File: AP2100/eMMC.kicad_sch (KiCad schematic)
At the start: 33 parts, among them U21 EMMC04G-M627-A01, U7 LS1043ASE7KQB-Layerscape

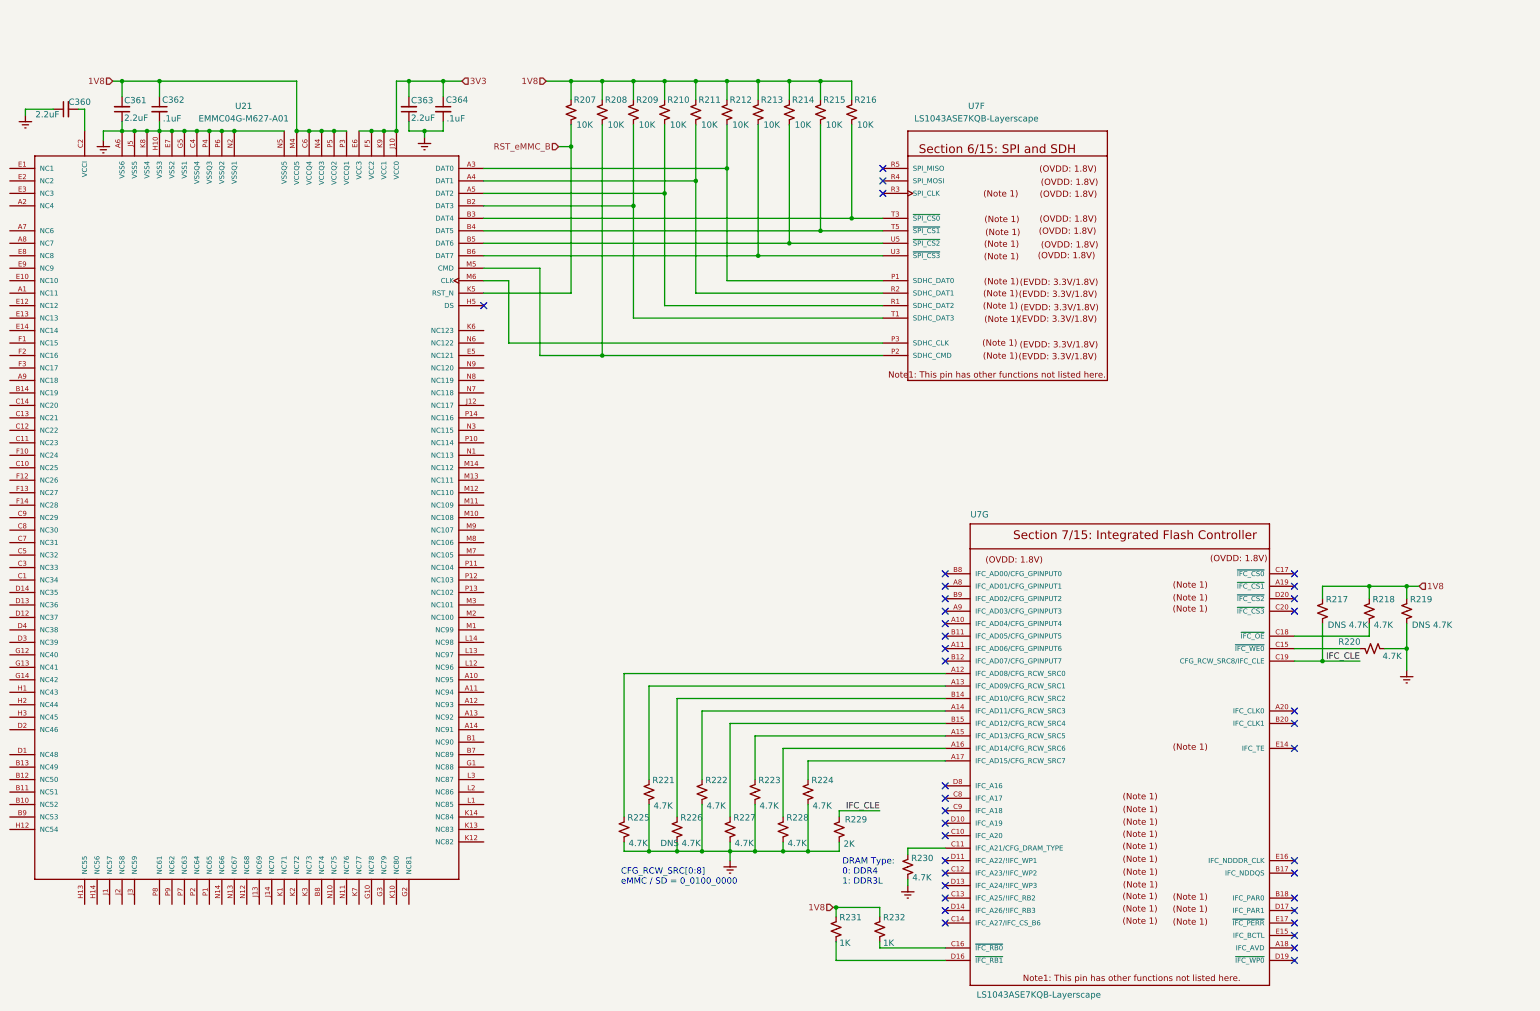
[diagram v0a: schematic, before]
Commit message: Added antenna mounting holes
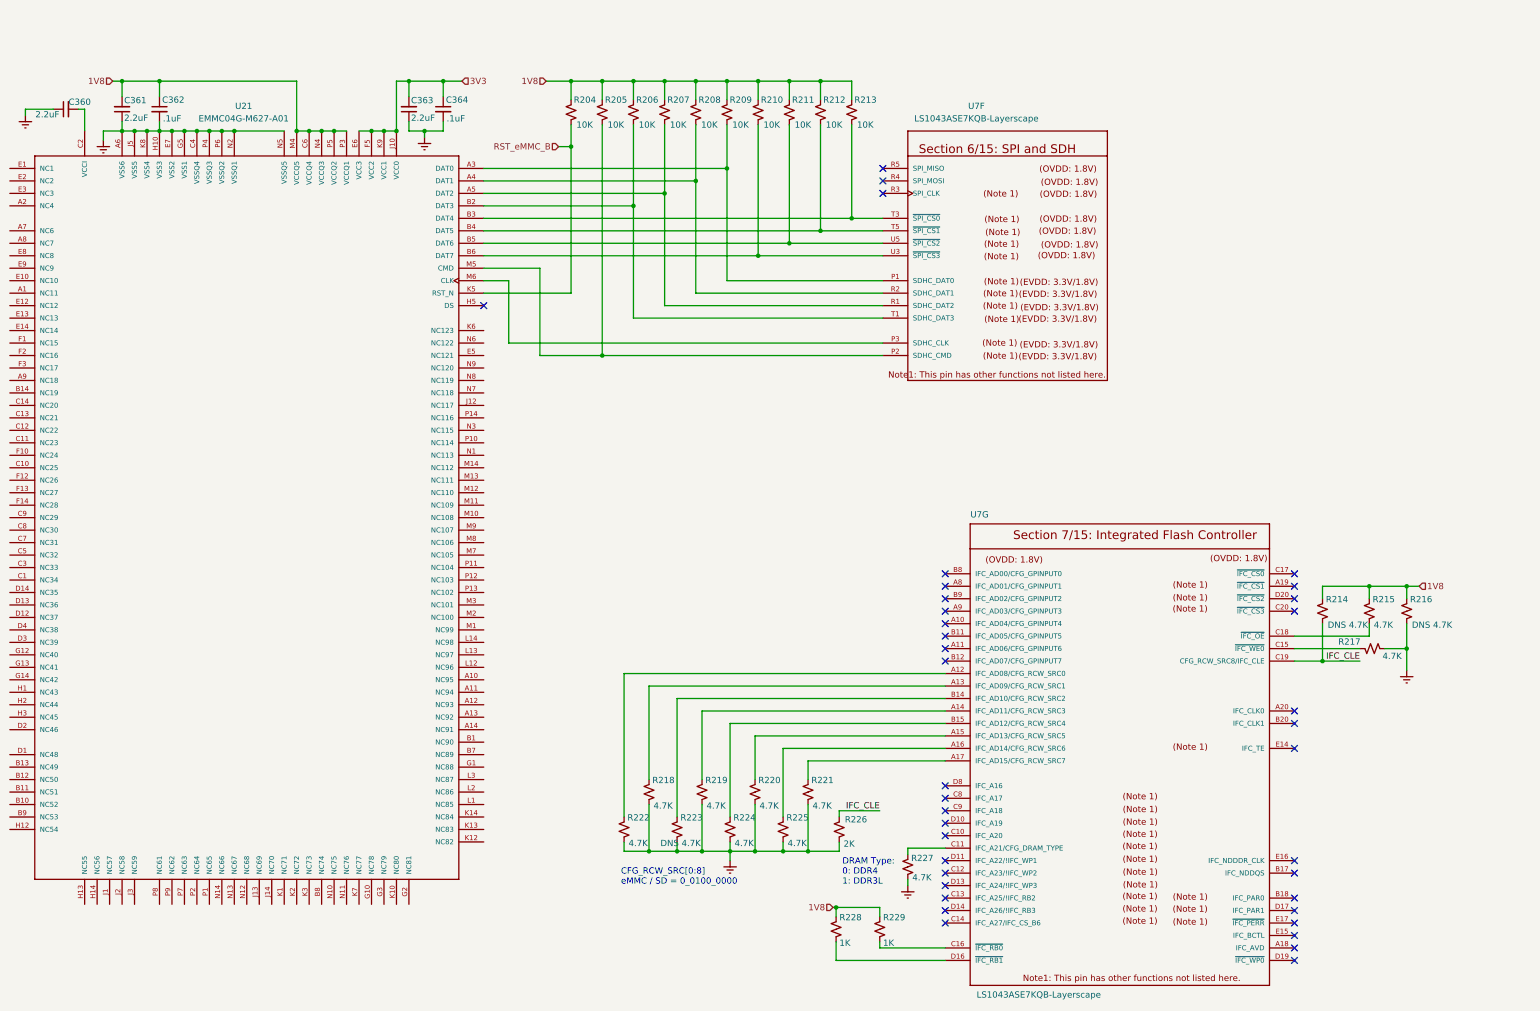
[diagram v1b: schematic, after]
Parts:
- renumbered R207 to R204, R208 to R205, R209 to R206, R210 to R207, R211 to R208, R212 to R209, R213 to R210, R214 to R211, R215 to R212, R216 to R213, R217 to R214, R218 to R215, R219 to R216, R220 to R217, R221 to R218, R222 to R219, R223 to R220, R224 to R221, R225 to R222, R226 to R223, R227 to R224, R228 to R225, R229 to R226, R230 to R227, R231 to R228, R232 to R229
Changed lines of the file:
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@@
   (symbol (lib_id "Device:R_Small_US") (at 167.64 46.99 0) (mirror y) (unit 1)
     (in_bom yes) (on_board yes)
-    (property "Reference" "R207" (id 0) (at 172.72 44.45 0)
+    (property "Reference" "R204" (id 0) (at 172.72 44.45 0)
       (effects (font (size 1.27 1.27)) (justify left))
     )
@@
   (symbol (lib_id "Device:R_Small_US") (at 173.99 46.99 0) (mirror y) (unit 1)
     (in_bom yes) (on_board yes)
-    (property "Reference" "R208" (id 0) (at 179.07 44.45 0)
+    (property "Reference" "R205" (id 0) (at 179.07 44.45 0)
       (effects (font (size 1.27 1.27)) (justify left))
     )
@@
   (symbol (lib_id "Device:R_Small_US") (at 178.435 193.04 0) (mirror y) (unit 1)
     (in_bom yes) (on_board yes)
-    (property "Reference" "R225" (id 0) (at 183.642 190.627 0)
+    (property "Reference" "R222" (id 0) (at 183.642 190.627 0)
       (effects (font (size 1.27 1.27)) (justify left))
     )
@@
   (symbol (lib_id "Device:R_Small_US") (at 180.34 46.99 0) (mirror y) (unit 1)
     (in_bom yes) (on_board yes)
-    (property "Reference" "R209" (id 0) (at 185.42 44.45 0)
+    (property "Reference" "R206" (id 0) (at 185.42 44.45 0)
       (effects (font (size 1.27 1.27)) (justify left))
     )
@@
   (symbol (lib_id "Device:R_Small_US") (at 183.515 185.42 0) (mirror y) (unit 1)
     (in_bom yes) (on_board yes)
-    (property "Reference" "R221" (id 0) (at 188.722 183.007 0)
+    (property "Reference" "R218" (id 0) (at 188.722 183.007 0)
       (effects (font (size 1.27 1.27)) (justify left))
     )
@@
   (symbol (lib_id "Device:R_Small_US") (at 186.69 46.99 0) (mirror y) (unit 1)
     (in_bom yes) (on_board yes)
-    (property "Reference" "R210" (id 0) (at 191.77 44.45 0)
+    (property "Reference" "R207" (id 0) (at 191.77 44.45 0)
       (effects (font (size 1.27 1.27)) (justify left))
     )
@@
   (symbol (lib_id "Device:R_Small_US") (at 189.23 193.04 0) (mirror y) (unit 1)
     (in_bom yes) (on_board yes)
-    (property "Reference" "R226" (id 0) (at 194.437 190.627 0)
+    (property "Reference" "R223" (id 0) (at 194.437 190.627 0)
       (effects (font (size 1.27 1.27)) (justify left))
     )
@@
   (symbol (lib_id "Device:R_Small_US") (at 193.04 46.99 0) (mirror y) (unit 1)
     (in_bom yes) (on_board yes)
-    (property "Reference" "R211" (id 0) (at 198.12 44.45 0)
+    (property "Reference" "R208" (id 0) (at 198.12 44.45 0)
       (effects (font (size 1.27 1.27)) (justify left))
     )
@@
   (symbol (lib_id "Device:R_Small_US") (at 194.31 185.42 0) (mirror y) (unit 1)
     (in_bom yes) (on_board yes)
-    (property "Reference" "R222" (id 0) (at 199.517 183.007 0)
+    (property "Reference" "R219" (id 0) (at 199.517 183.007 0)
       (effects (font (size 1.27 1.27)) (justify left))
     )
@@
   (symbol (lib_id "Device:R_Small_US") (at 199.39 46.99 0) (mirror y) (unit 1)
     (in_bom yes) (on_board yes)
-    (property "Reference" "R212" (id 0) (at 204.47 44.45 0)
+    (property "Reference" "R209" (id 0) (at 204.47 44.45 0)
       (effects (font (size 1.27 1.27)) (justify left))
     )
@@
   (symbol (lib_id "Device:R_Small_US") (at 200.025 193.04 0) (mirror y) (unit 1)
     (in_bom yes) (on_board yes)
-    (property "Reference" "R227" (id 0) (at 205.232 190.627 0)
+    (property "Reference" "R224" (id 0) (at 205.232 190.627 0)
       (effects (font (size 1.27 1.27)) (justify left))
     )
@@
   (symbol (lib_id "Device:R_Small_US") (at 205.105 185.42 0) (mirror y) (unit 1)
     (in_bom yes) (on_board yes)
-    (property "Reference" "R223" (id 0) (at 210.312 183.007 0)
+    (property "Reference" "R220" (id 0) (at 210.312 183.007 0)
       (effects (font (size 1.27 1.27)) (justify left))
     )
@@
   (symbol (lib_id "Device:R_Small_US") (at 205.74 46.99 0) (mirror y) (unit 1)
     (in_bom yes) (on_board yes)
-    (property "Reference" "R213" (id 0) (at 210.82 44.45 0)
+    (property "Reference" "R210" (id 0) (at 210.82 44.45 0)
       (effects (font (size 1.27 1.27)) (justify left))
     )
@@
   (symbol (lib_id "Device:R_Small_US") (at 210.82 193.04 0) (mirror y) (unit 1)
     (in_bom yes) (on_board yes)
-    (property "Reference" "R228" (id 0) (at 216.027 190.627 0)
+    (property "Reference" "R225" (id 0) (at 216.027 190.627 0)
       (effects (font (size 1.27 1.27)) (justify left))
     )
@@
   (symbol (lib_id "Device:R_Small_US") (at 212.09 46.99 0) (mirror y) (unit 1)
     (in_bom yes) (on_board yes)
-    (property "Reference" "R214" (id 0) (at 217.17 44.45 0)
+    (property "Reference" "R211" (id 0) (at 217.17 44.45 0)
       (effects (font (size 1.27 1.27)) (justify left))
     )
@@
   (symbol (lib_id "Device:R_Small_US") (at 215.9 185.42 0) (mirror y) (unit 1)
     (in_bom yes) (on_board yes)
-    (property "Reference" "R224" (id 0) (at 221.107 183.007 0)
+    (property "Reference" "R221" (id 0) (at 221.107 183.007 0)
       (effects (font (size 1.27 1.27)) (justify left))
     )
@@
   (symbol (lib_id "Device:R_Small_US") (at 218.44 46.99 0) (mirror y) (unit 1)
     (in_bom yes) (on_board yes)
-    (property "Reference" "R215" (id 0) (at 223.52 44.45 0)
+    (property "Reference" "R212" (id 0) (at 223.52 44.45 0)
       (effects (font (size 1.27 1.27)) (justify left))
     )
@@
   (symbol (lib_id "Device:R_Small_US") (at 221.615 213.36 0) (mirror y) (unit 1)
     (in_bom yes) (on_board yes)
-    (property "Reference" "R231" (id 0) (at 226.822 210.947 0)
+    (property "Reference" "R228" (id 0) (at 226.822 210.947 0)
       (effects (font (size 1.27 1.27)) (justify left))
     )
@@
   (symbol (lib_id "Device:R_Small_US") (at 222.25 193.04 0) (mirror x) (unit 1)
     (in_bom yes) (on_board yes)
-    (property "Reference" "R229" (id 0) (at 223.393 191.008 0)
+    (property "Reference" "R226" (id 0) (at 223.393 191.008 0)
       (effects (font (size 1.27 1.27)) (justify left))
     )
@@
   (symbol (lib_id "Device:R_Small_US") (at 224.79 46.99 0) (mirror y) (unit 1)
     (in_bom yes) (on_board yes)
-    (property "Reference" "R216" (id 0) (at 229.87 44.45 0)
+    (property "Reference" "R213" (id 0) (at 229.87 44.45 0)
       (effects (font (size 1.27 1.27)) (justify left))
     )
@@
   (symbol (lib_id "Device:R_Small_US") (at 230.505 213.36 0) (mirror y) (unit 1)
     (in_bom yes) (on_board yes)
-    (property "Reference" "R232" (id 0) (at 235.712 210.947 0)
+    (property "Reference" "R229" (id 0) (at 235.712 210.947 0)
       (effects (font (size 1.27 1.27)) (justify left))
     )
@@
   (symbol (lib_id "Device:R_Small_US") (at 236.22 200.66 0) (mirror y) (unit 1)
     (in_bom yes) (on_board yes)
-    (property "Reference" "R230" (id 0) (at 241.427 198.882 0)
+    (property "Reference" "R227" (id 0) (at 241.427 198.882 0)
       (effects (font (size 1.27 1.27)) (justify left))
     )
@@
   (symbol (lib_id "Device:R_Small_US") (at 320.675 148.59 0) (mirror y) (unit 1)
     (in_bom yes) (on_board yes)
-    (property "Reference" "R217" (id 0) (at 325.882 146.177 0)
+    (property "Reference" "R214" (id 0) (at 325.882 146.177 0)
       (effects (font (size 1.27 1.27)) (justify left))
     )
@@
   (symbol (lib_id "Device:R_Small_US") (at 330.2 148.59 0) (mirror y) (unit 1)
     (in_bom yes) (on_board yes)
-    (property "Reference" "R218" (id 0) (at 335.407 146.177 0)
+    (property "Reference" "R215" (id 0) (at 335.407 146.177 0)
       (effects (font (size 1.27 1.27)) (justify left))
     )
@@
   (symbol (lib_id "Device:R_Small_US") (at 330.835 156.21 90) (mirror x) (unit 1)
     (in_bom yes) (on_board yes)
-    (property "Reference" "R220" (id 0) (at 328.422 154.813 90)
+    (property "Reference" "R217" (id 0) (at 328.422 154.813 90)
       (effects (font (size 1.27 1.27)) (justify left))
     )
@@
   (symbol (lib_id "Device:R_Small_US") (at 337.82 148.59 0) (mirror y) (unit 1)
     (in_bom yes) (on_board yes)
-    (property "Reference" "R219" (id 0) (at 343.027 146.177 0)
-      (effects (font (size 1.27 1.27)) (justify left))
-    )
+    (property "Reference" "R216" (id 0) (at 343.027 146.177 0)
+      (effects (font (size 1.27 1.27)) (justify left))
+    )

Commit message: More cleanups
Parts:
- renumbered C360 to C378, C361 to C379, C362 to C380, C363 to C381, C364 to C382, R204 to R205, R205 to R206, R206 to R207, R207 to R208, R208 to R209, R209 to R210, R210 to R211, R211 to R212, R212 to R213, R213 to R214, R214 to R215, R215 to R216, R216 to R217, R217 to R218, R218 to R219, R219 to R220, R220 to R221, R221 to R222, R222 to R223, R223 to R224, R224 to R225, R225 to R226, R226 to R227, R227 to R228, R228 to R229, R229 to R230

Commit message: Not sure
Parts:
- U21: PartsBoxID (none) -> EMMC04G-M627-A01
- U7: value LS1043ASE7KQB-Layerscape -> LS1043ASE7xxx; PartsBoxID (none) -> LS1043ASE7
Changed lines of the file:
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@@
   (junction (at 337.82 143.51) (diameter 0.9144) (color 0 0 0 0))
   (junction (at 337.82 156.21) (diameter 0.9144) (color 0 0 0 0))
+  (no_connect (at 243.84 194.31))
+  (no_connect (at 314.96 143.51))
+  (no_connect (at 243.84 140.97))
+  (no_connect (at 243.84 143.51))
+  (no_connect (at 314.96 212.09))
+  (no_connect (at 231.14 58.42))
+  (no_connect (at 314.96 168.91))
+  (no_connect (at 243.84 156.21))
+  (no_connect (at 243.84 201.93))
+  (no_connect (at 314.96 219.71))
+  (no_connect (at 243.84 146.05))
+  (no_connect (at 243.84 191.77))
+  (no_connect (at 314.96 217.17))
+  (no_connect (at 231.14 63.5))
+  (no_connect (at 243.84 186.69))
+  (no_connect (at 243.84 158.75))
+  (no_connect (at 243.84 204.47))
+  (no_connect (at 243.84 184.15))
+  (no_connect (at 243.84 209.55))
+  (no_connect (at 314.96 199.39))
+  (no_connect (at 314.96 176.53))
+  (no_connect (at 231.14 60.96))
+  (no_connect (at 243.84 148.59))
+  (no_connect (at 314.96 148.59))
+  (no_connect (at 149.86 86.36))
+  (no_connect (at 243.84 189.23))
+  (no_connect (at 314.96 209.55))
+  (no_connect (at 243.84 212.09))
+  (no_connect (at 314.96 207.01))
+  (no_connect (at 243.84 207.01))
+  (no_connect (at 243.84 153.67))
+  (no_connect (at 243.84 151.13))
+  (no_connect (at 314.96 201.93))
+  (no_connect (at 314.96 146.05))
+  (no_connect (at 243.84 199.39))
+  (no_connect (at 314.96 214.63))
+  (no_connect (at 314.96 140.97))
   (no_connect (at 314.96 171.45))
-  (no_connect (at 314.96 146.05))
-  (no_connect (at 243.84 194.31))
-  (no_connect (at 314.96 199.39))
-  (no_connect (at 314.96 209.55))
-  (no_connect (at 243.84 158.75))
-  (no_connect (at 314.96 148.59))
-  (no_connect (at 314.96 217.17))
-  (no_connect (at 243.84 189.23))
-  (no_connect (at 314.96 212.09))
-  (no_connect (at 243.84 209.55))
-  (no_connect (at 314.96 207.01))
-  (no_connect (at 243.84 143.51))
-  (no_connect (at 243.84 201.93))
-  (no_connect (at 243.84 186.69))
-  (no_connect (at 243.84 153.67))
-  (no_connect (at 243.84 207.01))
-  (no_connect (at 243.84 191.77))
-  (no_connect (at 314.96 168.91))
-  (no_connect (at 243.84 151.13))
-  (no_connect (at 314.96 140.97))
-  (no_connect (at 314.96 143.51))
-  (no_connect (at 243.84 204.47))
-  (no_connect (at 314.96 176.53))
-  (no_connect (at 314.96 214.63))
-  (no_connect (at 243.84 184.15))
-  (no_connect (at 243.84 148.59))
-  (no_connect (at 231.14 63.5))
-  (no_connect (at 243.84 199.39))
-  (no_connect (at 314.96 219.71))
-  (no_connect (at 243.84 140.97))
-  (no_connect (at 314.96 201.93))
-  (no_connect (at 149.86 86.36))
-  (no_connect (at 243.84 212.09))
-  (no_connect (at 243.84 156.21))
-  (no_connect (at 243.84 146.05))
-  (no_connect (at 231.14 58.42))
-  (no_connect (at 231.14 60.96))
   (wire (pts (xy 56.515 46.355) (xy 56.515 47.625))
     (stroke (width 0) (type solid) (color 0 0 0 0))
@@
     (in_bom yes) (on_board yes)
     (property "Reference" "U7" (id 0) (at 250.19 45.72 0))
-    (property "Value" "LS1043ASE7KQB-Layerscape" (id 1) (at 250.19 48.26 0))
+    (property "Value" "LS1043ASE7xxx" (id 1) (at 250.19 48.26 0))
     (property "Footprint" "PLS1043ASE7QQA:BGA621C80P25X25_2100X2100X192N" (id 2) (at 254 77.47 0)
       (effects (font (size 1.27 1.27)) hide)
@@
       (effects (font (size 1.27 1.27)) hide)
     )
+    (property "PartsBoxID" "LS1043ASE7" (id 4) (at 254 77.47 0)
+      (effects (font (size 1.27 1.27)) hide)
+    )
   )
   (symbol (lib_id "AP2100-rescue:LS1043ASE7KQB-Layerscape") (at 279.4 177.8 0) (unit 7)
     (in_bom yes) (on_board yes)
     (property "Reference" "U7" (id 0) (at 250.825 128.905 0))
-    (property "Value" "LS1043ASE7KQB-Layerscape" (id 1) (at 262.89 226.695 0))
+    (property "Value" "LS1043ASE7xxx" (id 1) (at 262.89 226.695 0))
     (property "Footprint" "PLS1043ASE7QQA:BGA621C80P25X25_2100X2100X192N" (id 2) (at 279.4 177.8 0)
       (effects (font (size 1.27 1.27)) hide)
     )
     (property "Datasheet" "" (id 3) (at 279.4 177.8 0)
+      (effects (font (size 1.27 1.27)) hide)
+    )
+    (property "PartsBoxID" "LS1043ASE7" (id 4) (at 279.4 177.8 0)
       (effects (font (size 1.27 1.27)) hide)
     )
@@
       (effects (font (size 1.27 1.27)) (justify left bottom) hide)
     )
-  )
+    (property "PartsBoxID" "EMMC04G-M627-A01" (id 4) (at 101.6 129.54 0)
+      (effects (font (size 1.27 1.27)) hide)
+    )
+  )
